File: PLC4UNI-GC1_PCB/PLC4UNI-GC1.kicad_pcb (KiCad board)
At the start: 4 copper layers, 102.4 x 83.1 mm, 179 parts, among them J1 Conn_02x08_Odd_Even, K1 G5V-1, K2 G5V-1, Q1 NCE60P04R, Q2 ZXMS6004FFQTA, Q3 ZXMS6004FFQTA, Q4 ZXMS6004FFQTA, Q5 ZXMS6004FFQTA, SW1 TS-1088-AR02016, U1 ESP32-S3-WROOM-1, U10 ADS1115IDGS, U11 AT3H4B-CUH-S, U12 AT3H4B-CUH-S, U13 LK1802, U14 AT3H4B-CUH-S, U15 MAX31856MUD+, U16 BL0942, U17 B0303S-1WR3_C7465185, U18 ISO7021DR, U2 AT3H4B-CUH-S, U3 AP63203WU, U4 RS485-PROTECT, U5 AT3H4B-CUH-S, U6 AT3H4B-CUH-S, U7 GP8211S-TC50-EW, U8 GP8302-TC50-EW, U9 BTS723GWXUMA1

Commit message: update of gnd2
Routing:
- net /control/IN-4-20MA1/OUT: track 8.86 -> 27.1 mm, vias 0 -> 2
- net /control/IN-4-20MA/OUT: track 11.3 -> 29.5 mm, vias 0 -> 1
- net /control/i2c_scl: track 27.1 -> 43.9 mm, vias 2 -> 3

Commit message: update of pcb design
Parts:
- moved C1 2.88 mm to (126.1, 114.0)
- moved U10 1.45 mm to (156.0, 106.6), turned to 180 degrees
- moved C37 0.76 mm to (166.7, 83.2)
- moved U16 0.74 mm to (170.3, 83.3)
- moved TP11 0.56 mm to (166.1, 78.9)
- moved D10 0.13 mm to (156.7, 75.4)
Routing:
- net /control/OUT_NPN1: track 0.00 -> 45.1 mm, vias 0 -> 2
- net /control/CON_RS485_G: track 0.00 -> 11.9 mm
- net /control/i2c_sda: track 69.9 -> 58.3 mm
- net /control/i2c_scl: track 43.9 -> 32.9 mm, vias 3 -> 2
- net /control/CON_RS485_A: track 0.00 -> 10.9 mm
- net Net-(LED3-A): track 0.00 -> 9.90 mm
- net /control/CON_RS485_B: track 0.94 -> 10.8 mm
- net +3.3V: track 33.5 -> 41.2 mm, vias 34 -> 42
- net /control/IN-4-20MA1/OUT: track 27.1 -> 20.7 mm, vias 2 -> 0
- net /control/IN-4-20MA/OUT: track 29.5 -> 24.9 mm
- net GND: track 60.6 -> 64.9 mm, vias 97 -> 100
- net /control/CON_OUT_NPN1: track 11.9 -> 14.9 mm
- net /control/IN-0-10V/OUT3V: track 40.0 -> 37.8 mm

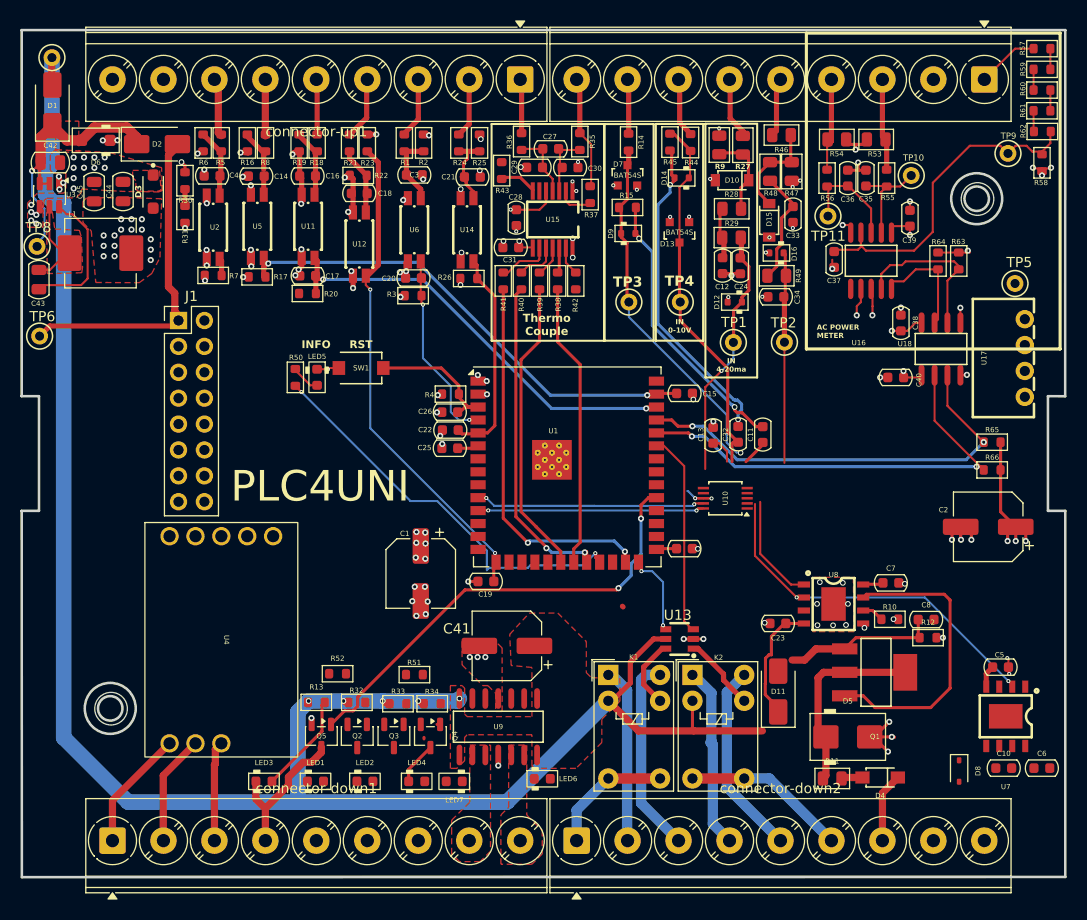
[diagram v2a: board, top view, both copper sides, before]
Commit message: update power routing
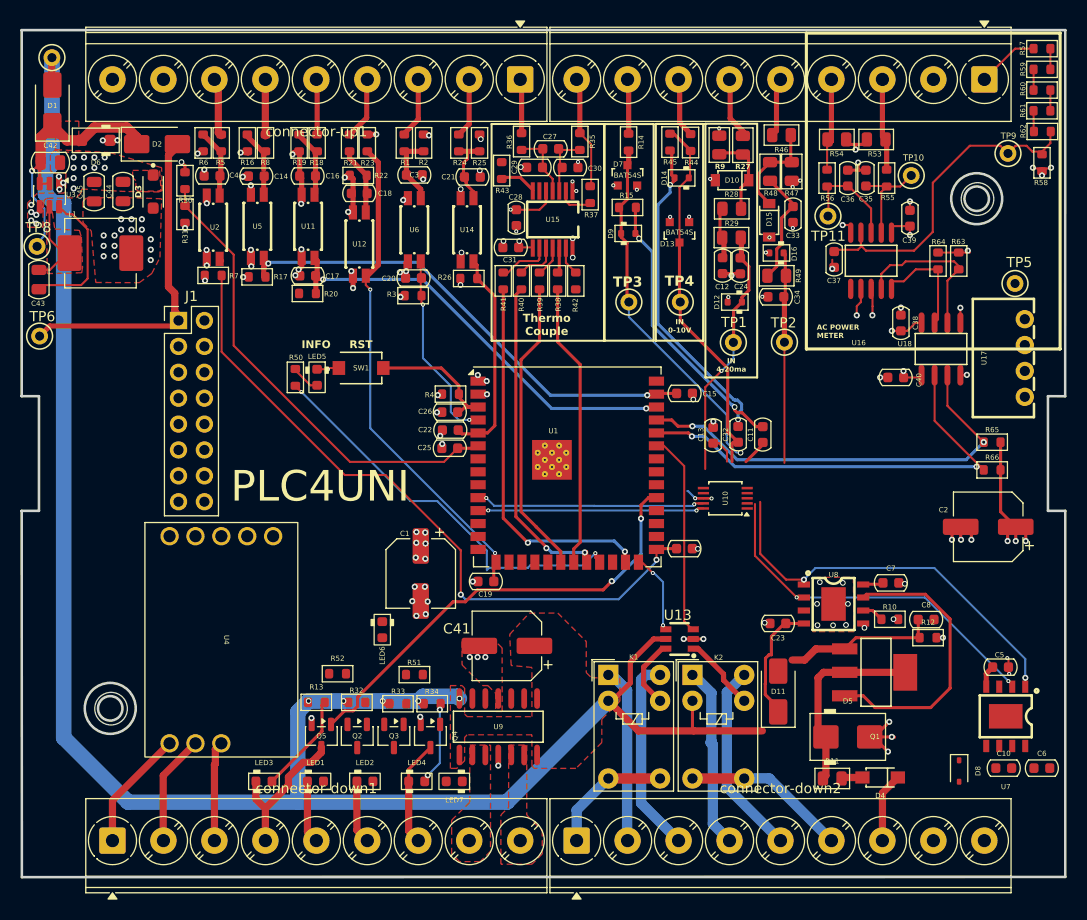
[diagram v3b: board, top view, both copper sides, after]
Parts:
- moved LED6 21.5 mm to (122.4, 119.5), turned to -90 degrees
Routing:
- net /control/IN_NPN1: track 4.08 -> 68.1 mm, vias 0 -> 2
- net /control/IN_VDC_ADC: track 3.75 -> 46.7 mm
- net /control/i2c_scl: track 32.9 -> 61.8 mm, vias 2 -> 4
- net Net-(LED4-A): track 0.00 -> 8.27 mm, vias 0 -> 2
- net /control/CON_OUT_NPN3: track 0.00 -> 6.24 mm
- net /control/CON_OUT_NPN4: track 4.20 -> 10.4 mm
- net /control/CON_OUT_NPN2: track 0.00 -> 6.17 mm
- net Net-(U8-IOUT): track 29.1 -> 28.0 mm
- net /control/OUT_NPN1: track 45.1 -> 44.5 mm
- net GND: track 64.9 -> 65.2 mm, vias 100 -> 101
